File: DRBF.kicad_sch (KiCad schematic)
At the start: 94 parts, among them J1 VER-A, J10 INV-A, J11 INV-B, J2 In-A, J3 In-AB, J4 In-B, J5 Eurorack_Power, J6 VER-B, J7 Out-A, J8 Out-AB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

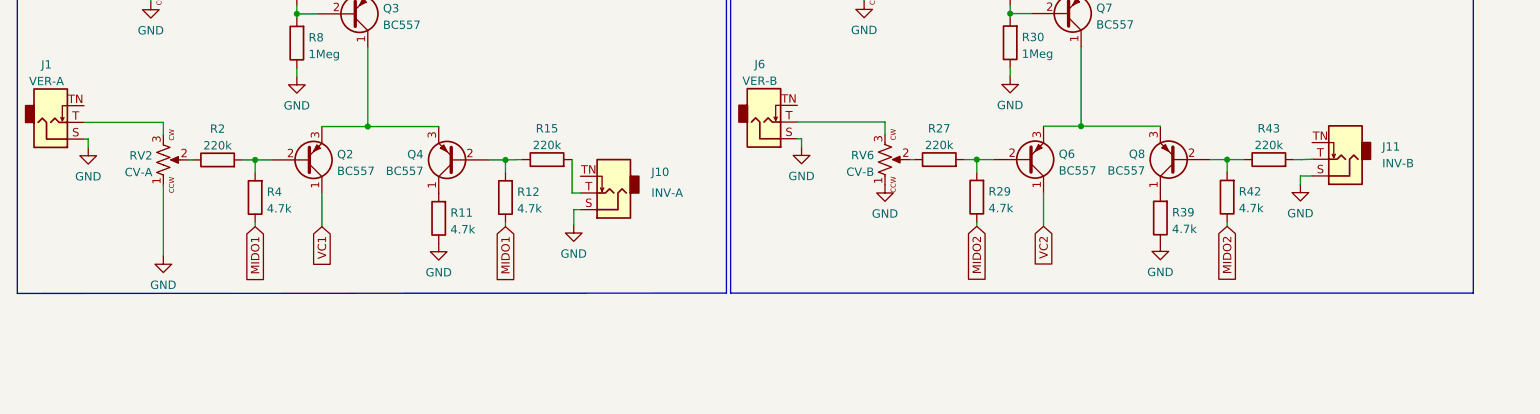
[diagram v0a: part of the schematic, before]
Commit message: Added negative voltage protection diodes
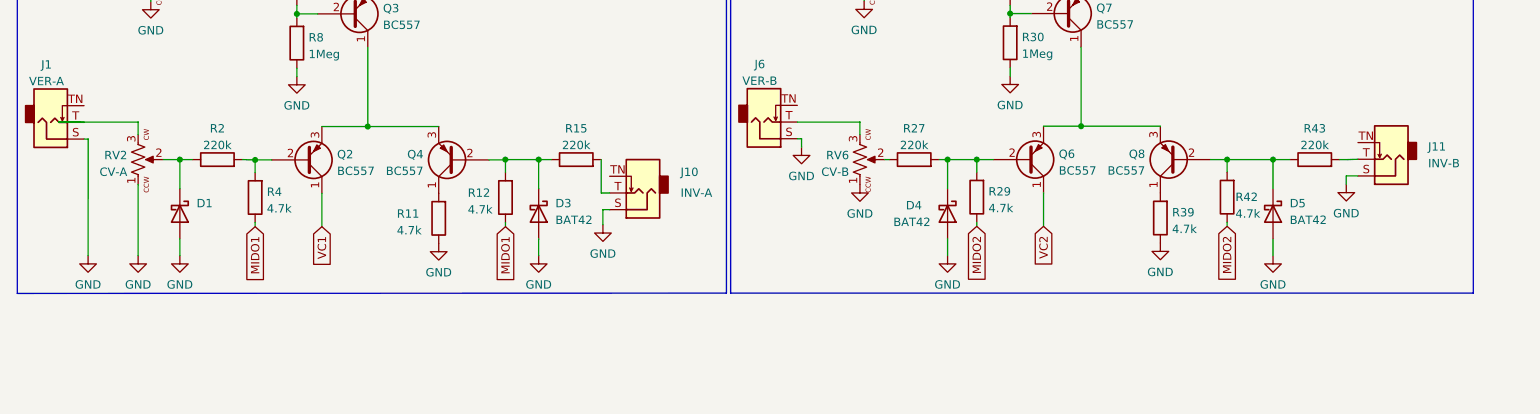
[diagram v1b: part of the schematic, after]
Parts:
- added D1: (no value), symbol Diode:BAT42
- added D3, D4, D5: BAT42, Diode_THT:D_DO-35_SOD27_P7.62mm_Horizontal, symbol Diode:BAT42
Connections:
- net GND: now also D1.2 (A), D3.2 (A), D4.2 (A), D5.2 (A)
- net at Q4.2 (B), R12.2: no longer R15.1
- net at Q8.2 (B), R42.2, R43.1: now also D5.1 (K)
- net at Q6.2 (B), R27.2, R29.2: now also D4.1 (K)
- net at R2.1, RV2.2: now also D1.1 (K)
- new net: D3.1 (K), R15.1
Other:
- moved on the sheet: J10, J11, R15, R27, R43, RV2, RV6
